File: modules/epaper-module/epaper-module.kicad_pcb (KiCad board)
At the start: 2 copper layers, 33 x 63.5 mm, 32 parts, among them J1 Conn_01x04, J2 Conn_01x04, Q1 Si1308EDL, U2 MIC5504-3.3YM5, U3 TXS0108EPW

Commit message: EPaper module: reorganize schematic
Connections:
- net Net-(C10-Pad1) renamed /VSL
- net Net-(C11-Pad1) renamed /PREVGL
- net Net-(C12-Pad1) renamed /VCOM
- net Net-(C2-Pad1) renamed /VSH2
- net Net-(C5-Pad1) renamed /PREVGH
- net Net-(C7-Pad1) renamed /VDD
- net Net-(C9-Pad1) renamed /VSH1
- net Net-(Q1-Pad1) renamed /GDR
- net Net-(Q1-Pad2) renamed /RESE

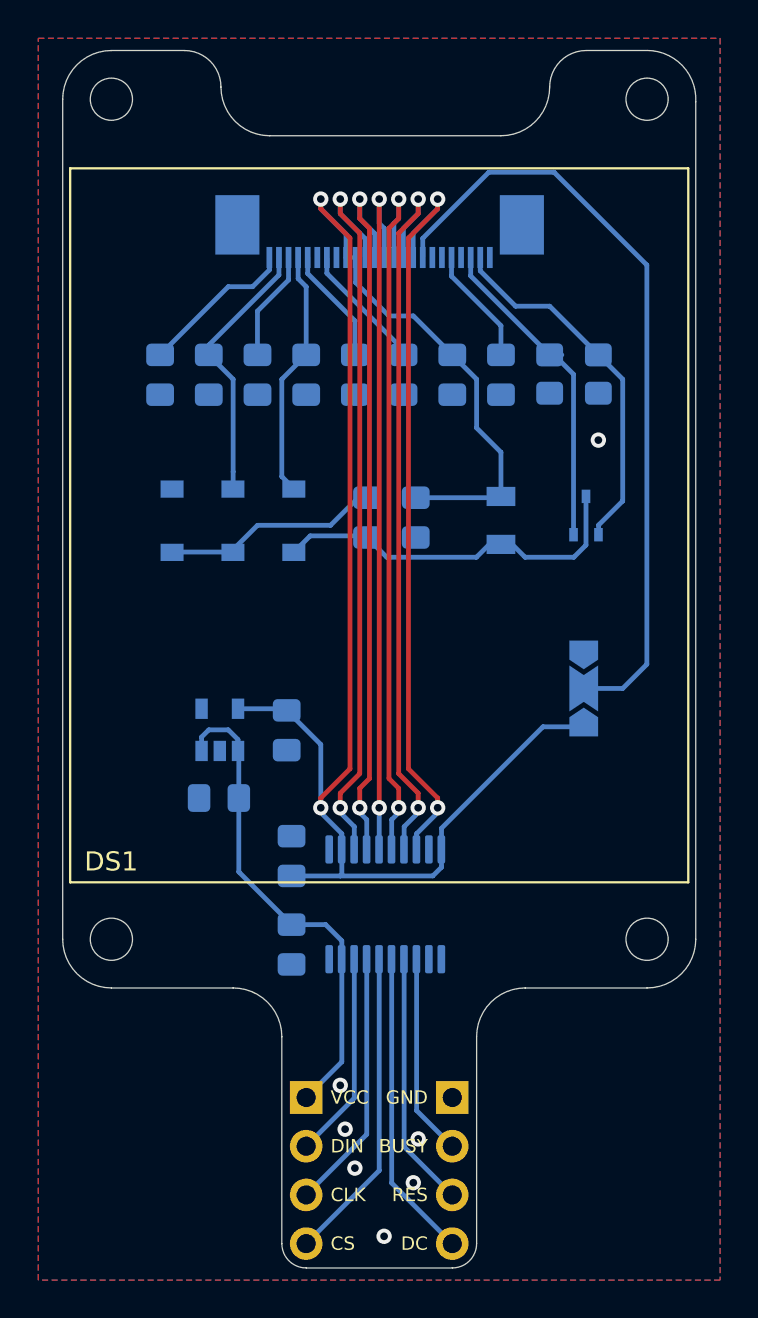
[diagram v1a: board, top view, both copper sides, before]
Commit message: EPaper module: add two capacitors from Waveshare module schematic
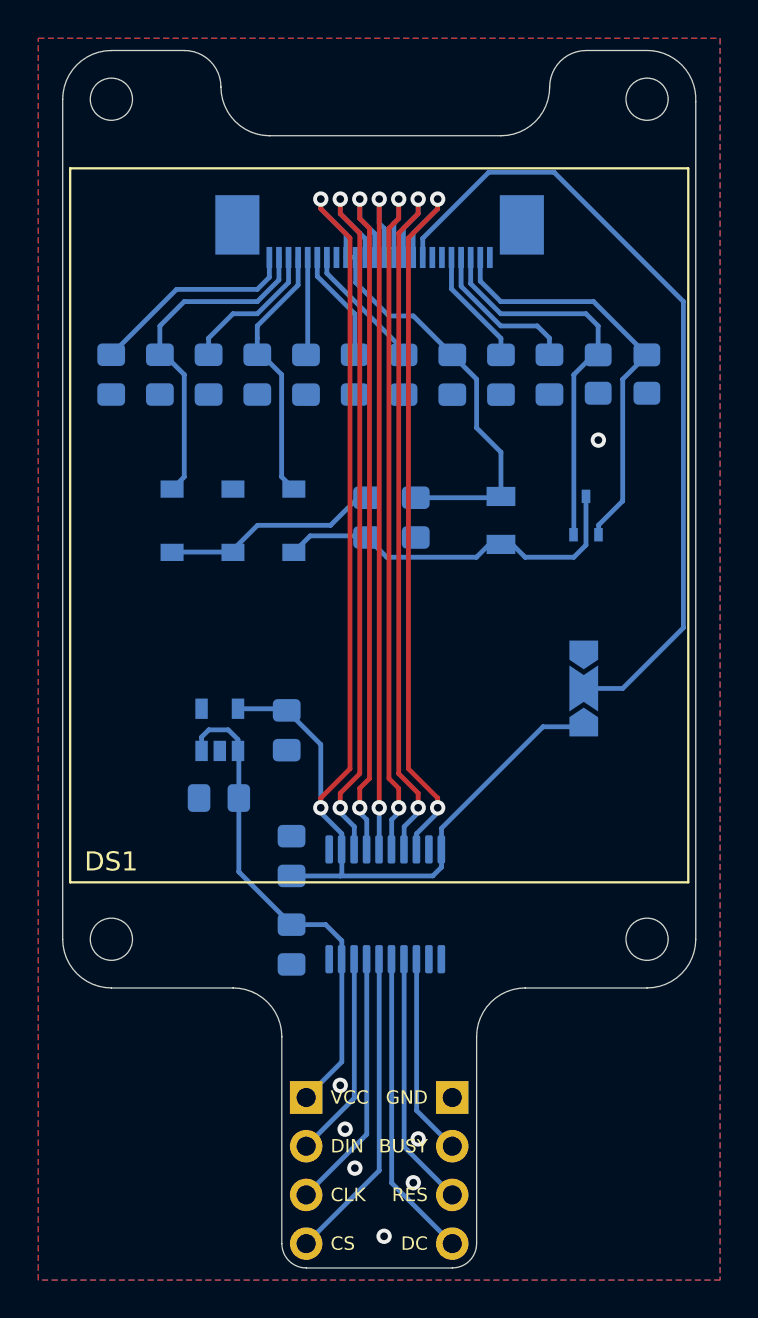
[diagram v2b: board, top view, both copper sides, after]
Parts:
- added C15: 1uF, Capacitor_SMD:C_0805_2012Metric_Pad1.18x1.45mm_HandSolder, B.Cu at (153.8, 84.2)
- added C16: 1uF, Capacitor_SMD:C_0805_2012Metric_Pad1.18x1.45mm_HandSolder, B.Cu at (163.9, 84.2)
- moved D1 3.18 mm to (144.3, 91.8)
- moved D2 3.18 mm to (147.4, 91.8)
- moved C10 2.55 mm to (146.2, 84.2)
- moved C12 2.55 mm to (141.1, 84.2)
- moved C5 2.55 mm to (148.7, 84.2)
- moved C11 2.55 mm to (143.6, 84.2)
- moved C9 2.55 mm to (151.2, 84.2)
- moved R2 2.53 mm to (166.5, 84.2)
- moved R1 2.53 mm to (169.0, 84.2)
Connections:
- XDS1 pad 21: (no net) -> Net-(C16-Pad1)
- XDS1 pad 6: (no net) -> Net-(C15-Pad1)
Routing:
- net Net-(C16-Pad1): track 0.00 -> 8.50 mm
- net Net-(C15-Pad1): track 0.00 -> 5.88 mm
- net /PREVGL: track 14.1 -> 17.8 mm
- net /VCOM: track 8.18 -> 11.4 mm
- net /RESE: track 17.5 -> 20.5 mm
- net /GDR: track 19.1 -> 21.9 mm
- net /VSL: track 5.75 -> 8.05 mm
- net /BS: track 40.8 -> 42.3 mm
- net /VSH1: track 6.10 -> 5.12 mm
- net /PREVGH: track 13.0 -> 13.9 mm

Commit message: EPaper module: reannotate schematic
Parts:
- renumbered C16 to C1, C12 to C10, C4 to C11, C3 to C12, C1 to C13, C8 to C14, C14 to C15, C13 to C16, C6 to C3, C7 to C4, C15 to C5, C9 to C6, C5 to C7, C10 to C8, C11 to C9, U2 to U1, U3 to U2
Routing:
- net /BS: track 42.3 -> 35.7 mm, vias 0 -> 2
